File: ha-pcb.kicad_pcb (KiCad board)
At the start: 2 copper layers, 137.2 x 111.8 mm, 52 parts, among them J1 RJ45_NC1W, J10 1VAC_00, J11 1VAC_01, J12 5VCC_02, J13 5VCC_03, J14 30VCC_11, J15 ONOFF_134, J16 I2C_5V, J17 locked, J2 RaPi_Connector, J3 RJ45_NC1W, J4 SainSmart_connector, J5 RJ45_1W1W, J6 RJ45_1W1W, J7 RJ45_1W1W, J8 RJ45_1W1W_T, J9 locked, U1 DMO063_SSR, U10 ADS1115 ADC, U11 ADS1115, U2 PCF_8575, U3 AK-DS2482S-100, U4 Pololu_Level_Shifter, U5 DS18B20, U6 PCA9615_I2C_Diff, U7 AK-DS2482S-100, U8 AK-DS2482S-100, U9 AK-DS2482S-100

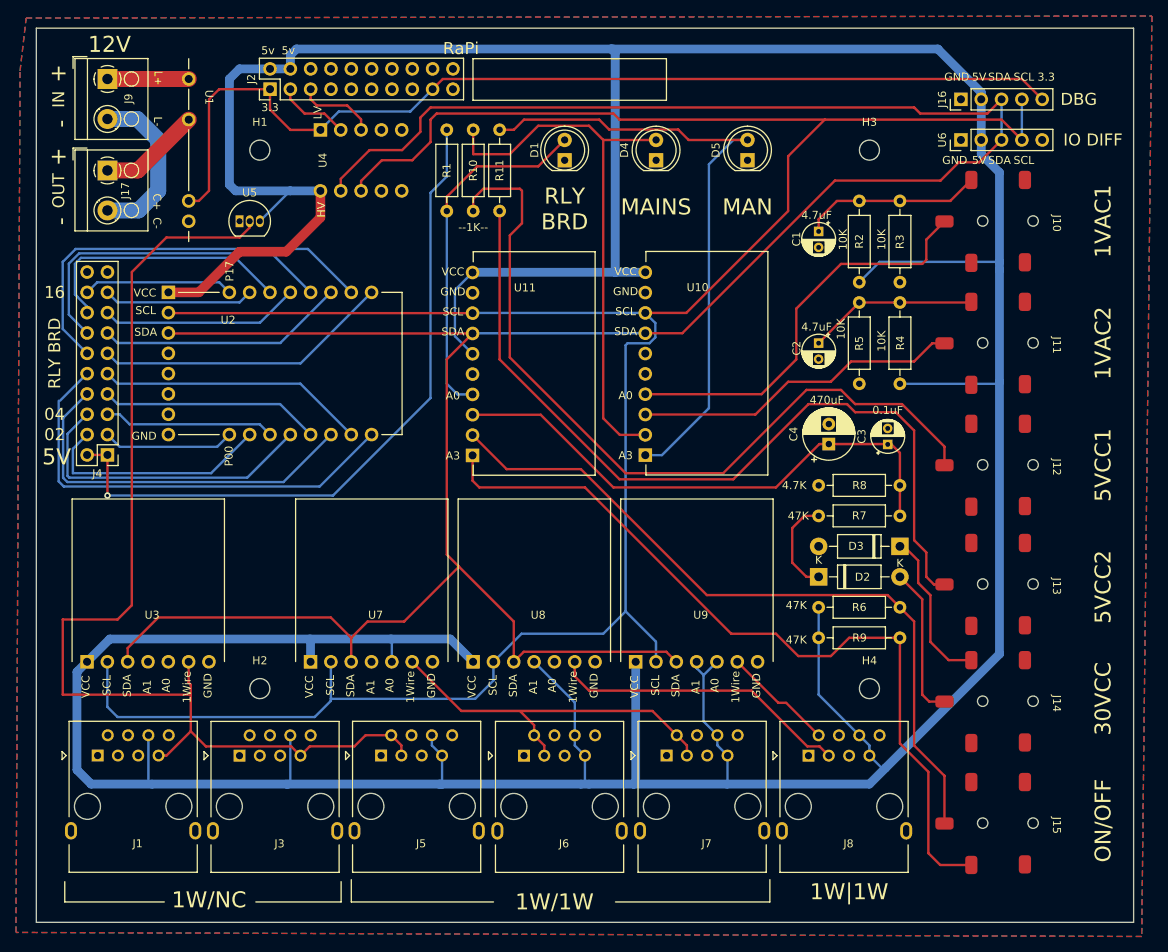
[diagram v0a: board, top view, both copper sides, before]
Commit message: Incorporated feedback from forum.\nAdded two GPIOs for test marking
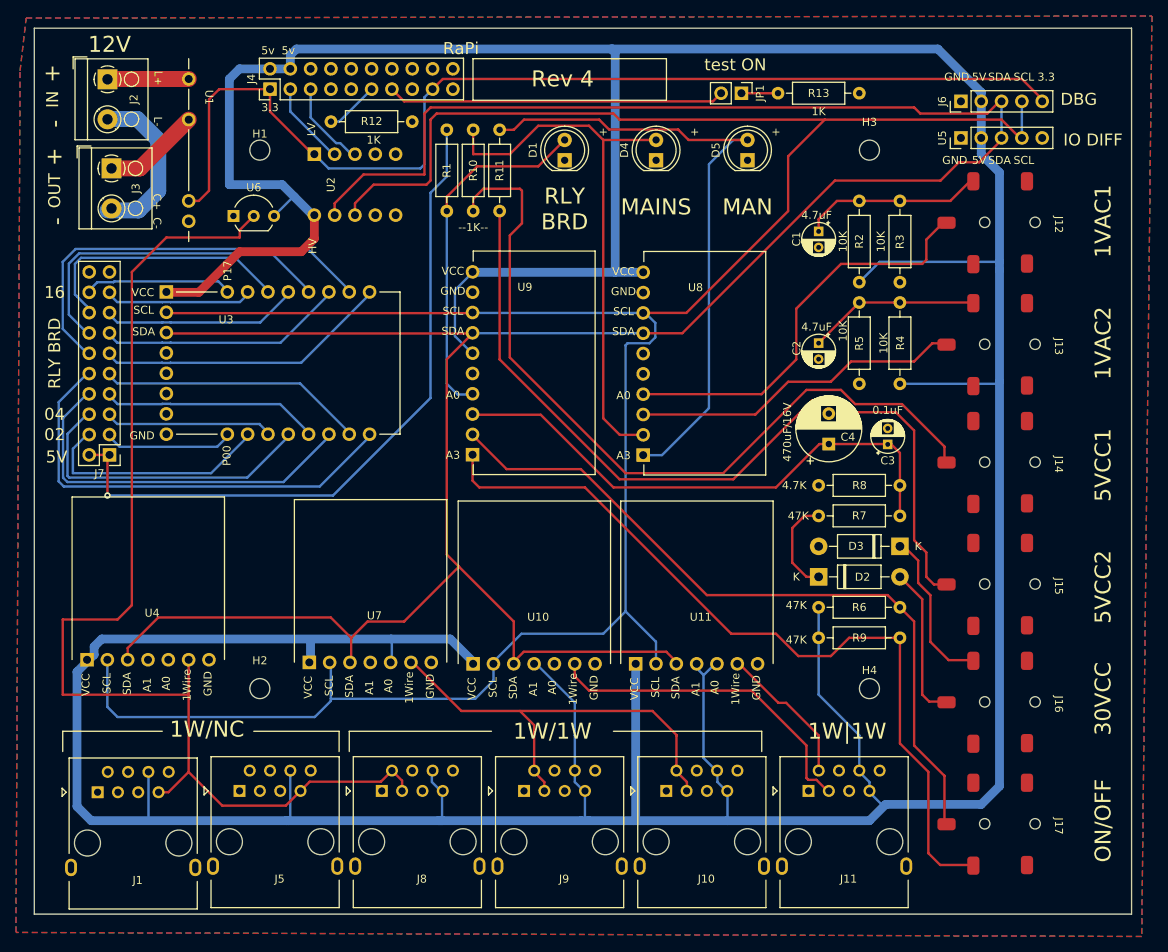
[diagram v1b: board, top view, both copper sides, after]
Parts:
- added JP1: Jumper_2_Open, Connector_PinHeader_2.54mm:PinHeader_1x02_P2.54mm_Vertical, F.Cu at (129.0, 39.6)
- added R12: 1K, Resistor_THT:R_Axial_DIN0207_L6.3mm_D2.5mm_P10.16mm_Horizontal, F.Cu at (77.7, 43.2)
- added R13: 1K, Resistor_THT:R_Axial_DIN0207_L6.3mm_D2.5mm_P10.16mm_Horizontal, F.Cu at (133.6, 39.6)
- C4: value 470uF -> 470uF/16V; footprint Capacitor_THT:CP_Radial_D6.3mm_P2.50mm -> Capacitor_THT:CP_Radial_D8.0mm_P3.80mm
- D1: value yellow -> LED; footprint LED_THT:LED_D5.0mm_IRGrey -> LED_THT:LED_D5.0mm
- D4, D5: value yellow -> LED
- J10: value 1VAC_00 -> RJ45_1W1W; footprint Library:3.5mmJack SMD -> Library:RJ45_Ninigi_GE_silver
- J11: value 1VAC_01 -> RJ45_1W1W; footprint Library:3.5mmJack SMD -> Library:RJ45_Ninigi_GE_silver
- J12: value 5VCC_02 -> 3.5Inch_Audio
- J13: value 5VCC_03 -> 3.5Inch_Audio
- J14: value 30VCC_11 -> 3.5Inch_Audio
- J15: value ONOFF_134 -> 3.5Inch_Audio
- J16: value I2C_5V -> 3.5Inch_Audio; footprint Connector_PinHeader_2.54mm:PinHeader_1x05_P2.54mm_Vertical -> Library:3.5mmJack SMD
- J17: footprint TerminalBlock_RND:TerminalBlock_RND_205-00001_1x02_P5.00mm_Horizontal -> Library:3.5mmJack SMD
- J2: value RaPi_Connector -> 12V IN; footprint Connector_PinHeader_2.54mm:PinHeader_2x10_P2.54mm_Vertical -> TerminalBlock_RND:TerminalBlock_RND_205-00001_1x02_P5.00mm_Horizontal
- J3: value RJ45_NC1W -> 12V OUT; footprint Library:RJ45_Ninigi_GE_silver -> TerminalBlock_RND:TerminalBlock_RND_205-00001_1x02_P5.00mm_Horizontal
- J4: value SainSmart_connector -> RaPi_Connector
- J5: value RJ45_1W1W -> RJ45_NC1W
- J6: value RJ45_1W1W -> Conn_01x05; footprint Library:RJ45_Ninigi_GE_silver -> Connector_PinHeader_2.54mm:PinHeader_1x05_P2.54mm_Vertical
- J7: value RJ45_1W1W -> SainSmart_connector; footprint Library:RJ45_Ninigi_GE_silver -> Connector_PinHeader_2.54mm:PinHeader_2x10_P2.54mm_Vertical
- J8: value RJ45_1W1W_T -> RJ45_1W1W
- J9: footprint TerminalBlock_RND:TerminalBlock_RND_205-00001_1x02_P5.00mm_Horizontal -> Library:RJ45_Ninigi_GE_silver
- U10: value ADS1115 ADC -> AK-DS2482S-100; footprint Library:ADS1115 -> Library:AK-DS2482S-100
- U11: value ADS1115 -> AK-DS2482S-100; footprint Library:ADS1115 -> Library:AK-DS2482S-100
- U2: value PCF_8575 -> Pololu_Level_Shifter; footprint Library:PCF_8575 -> Library:Pololu Level Shifter
- U3: value AK-DS2482S-100 -> PCF_8575; footprint Library:AK-DS2482S-100 -> Library:PCF_8575
- U4: value Pololu_Level_Shifter -> AK-DS2482S-100; footprint Library:Pololu Level Shifter -> Library:AK-DS2482S-100
- U5: value DS18B20 -> PCA9615_I2C_Diff; footprint Package_TO_SOT_THT:TO-92_Inline -> Connector_PinHeader_2.54mm:PinHeader_1x05_P2.54mm_Vertical
- U6: value PCA9615_I2C_Diff -> DS18B20; footprint Connector_PinHeader_2.54mm:PinHeader_1x05_P2.54mm_Vertical -> Package_TO_SOT_THT:TO-92_Inline_Wide
- U8, U9: value AK-DS2482S-100 -> ADS1115; footprint Library:AK-DS2482S-100 -> Library:ADS1115
- moved J17 137.8 mm to (167.8, 120.5)
- moved J9 103.1 mm to (101.9, 126.8), turned to 0 degrees
- moved J6 98.3 mm to (156.5, 40.6), turned to 90 degrees
- moved J10 94.7 mm to (119.6, 126.8), turned to 0 degrees
- moved U6 91.4 mm to (65.5, 55.0), turned to 0 degrees
- moved U5 90.8 mm to (156.5, 45.2), turned to 90 degrees
- moved J7 79.1 mm to (50.0, 84.8), turned to 180 degrees
- moved J3 75.1 mm to (50.3, 49.0), turned to -90 degrees
- moved J11 73.0 mm to (137.4, 126.8), turned to 0 degrees
- moved J16 65.8 mm to (167.8, 105.2), turned to -90 degrees
- moved J8 53.5 mm to (84.1, 126.8)
- moved J4 50.0 mm to (70.1, 39.1), turned to 90 degrees
- moved U4 47.5 mm to (45.4, 90.1), turned to 0 degrees
- moved U11 37.6 mm to (113.9, 90.6)
- moved U10 37.6 mm to (93.6, 90.6)
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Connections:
- C3 pad 1: Net-(C3-Pad1) -> /A2/1
- C4 pad 1: Net-(C3-Pad1) -> /A2/1
- D1 pad 2: /5VRB -> /A2/0
- D4 pad 2: Net-(D4-Pad2) -> /A1/2
- D5 pad 2: Net-(D5-Pad2) -> /A1/3
- J1 pad SH: (no net) -> GND
- J10 pad 1: Net-(C1-Pad1) -> GND
- J10 pad 3: unconnected-(J10-Pad3) -> Net-(J10-Pad2)
- J10 pad 4: (no net) -> GND
- J10 pad 5: (no net) -> GND
- J11 pad 1: Net-(C2-Pad1) -> GND
- J11 pad 3: unconnected-(J11-Pad3) -> Net-(J11-Pad3)
- J11 pad 4: (no net) -> GND
- J11 pad 5: (no net) -> GND
- J12 pad 1: GND -> Net-(C1-Pad1)
- J12 pad 2: Net-(J12-Pad2) -> /A1/0
- J12 pad 4: (no net) -> GND
- J12 pad 5: (no net) -> GND
- J13 pad 1: GND -> Net-(C2-Pad1)
- J13 pad 2: Net-(J13-Pad2) -> /A1/1
- J13 pad 4: (no net) -> GND
- J13 pad 5: (no net) -> GND
- J14 pad 1: Net-(D3-Pad1) -> GND
- J14 pad 2: Net-(D2-Pad2) -> Net-(J14-Pad2)
- J14 pad 4: (no net) -> GND
- J14 pad 5: (no net) -> GND
- J15 pad 3: Net-(J15-Pad3) -> unconnected-(J15-Pad3)
- J15 pad 4: (no net) -> GND
- J15 pad 5: (no net) -> GND
- J16 pad 1: GND -> Net-(D3-Pad1)
- J16 pad 2: +5V -> Net-(D2-Pad2)
- J16 pad 3: /SDA -> unconnected-(J16-Pad3)
- J16 pad 4: /SCL -> GND
- J16 pad 5: /+3.3V -> GND
- J17 pad 1: Net-(J17-Pad1) -> GND
- J17 pad 2: Net-(J17-Pad2) -> /A2/2
- J2 pad 1: /+3.3V -> Net-(J2-Pad1)
- J2 pad 2: +5V -> Net-(J2-Pad2)
- J3 pad 1: unconnected-(J3-Pad1) -> Net-(J3-Pad1)
- J3 pad 2: unconnected-(J3-Pad2) -> Net-(J2-Pad2)
- J4 pad 1: /5VSS -> /+3.3V
- J4 pad 10: Net-(J4-Pad10) -> unconnected-(J4-Pad10)
- J4 pad 12: Net-(J4-Pad12) -> unconnected-(J4-Pad12)
- J4 pad 14: Net-(J4-Pad14) -> GND
- J4 pad 15: Net-(J4-Pad15) -> unconnected-(J4-Pad15)
- J4 pad 16: Net-(J4-Pad16) -> unconnected-(J4-Pad16)
- J4 pad 17: /R15 -> /+3.3V
- J4 pad 18: /R16 -> unconnected-(J4-Pad18)
- J4 pad 19: GND -> unconnected-(J4-Pad19)
- J4 pad 2: /5VSS -> +5V
- J4 pad 3: /R01 -> /SDA_L
- J4 pad 4: /R02 -> +5V
- J4 pad 5: Net-(J4-Pad5) -> /SCL_L
- J4 pad 6: Net-(J4-Pad6) -> GND
- J4 pad 7: Net-(J4-Pad7) -> unconnected-(J4-Pad7)
- J4 pad 8: Net-(J4-Pad8) -> unconnected-(J4-Pad8)
- J4 pad 9: Net-(J4-Pad9) -> GND
- J5 pad 1: GND -> unconnected-(J5-Pad1)
- J5 pad 2: Net-(J1-Pad7) -> unconnected-(J5-Pad2)
- J5 pad 3: Net-(J1-Pad7) -> unconnected-(J5-Pad3)
- J5 pad 4: GND -> unconnected-(J5-Pad4)
- J5 pad 7: +5V -> Net-(J1-Pad7)
- J5 pad SH: (no net) -> GND
- J6 pad 2: Net-(J6-Pad2) -> +5V
- J6 pad 3: Net-(J6-Pad2) -> /SDA
- J6 pad 4: GND -> /SCL
- J6 pad 5: GND -> /+3.3V
- J7 pad 1: GND -> /5VSS
- J7 pad 2: Net-(J6-Pad2) -> /5VSS
- J7 pad 3: Net-(J6-Pad2) -> /R01
- J7 pad 4: GND -> /R02
- J7 pad 5: GND -> Net-(J7-Pad5)
- J7 pad 6: +5V -> Net-(J7-Pad6)
- J7 pad 7: +5V -> Net-(J7-Pad7)
- J7 pad 8: GND -> Net-(J7-Pad8)
- J8 pad 2: Net-(J8-Pad2) -> Net-(J1-Pad7)
- J8 pad 3: Net-(J8-Pad3) -> Net-(J1-Pad7)
- J8 pad SH: (no net) -> GND
- J9 pad 1: Net-(J9-Pad1) -> GND
- J9 pad 2: Net-(J17-Pad2) -> Net-(J10-Pad2)
- R1 pad 2: /5VRB -> /A2/0
- R10 pad 1: Net-(D4-Pad2) -> /A1/2
- R10 pad 2: Net-(J12-Pad2) -> Net-(J14-Pad2)
- R11 pad 1: Net-(D5-Pad2) -> /A1/3
- R11 pad 2: Net-(J13-Pad2) -> Net-(J15-Pad2)
- R6 pad 1: Net-(J15-Pad2) -> /A2/2
- R7 pad 1: Net-(C3-Pad1) -> /A2/1
- R8 pad 2: Net-(C3-Pad1) -> /A2/1
- R9 pad 1: Net-(J15-Pad3) -> /A2/3
- U1 pad 1: Net-(J9-Pad1) -> Net-(J2-Pad1)
- U1 pad 2: Net-(J17-Pad1) -> Net-(J3-Pad1)
- U10 pad 1: Net-(D5-Pad2) -> +5V
- U10 pad 2: Net-(D4-Pad2) -> /SCL
- U10 pad 3: Net-(J11-Pad2) -> /SDA
- U10 pad 4: Net-(J10-Pad2) -> +5V
- U10 pad 6: GND -> Net-(J11-Pad3)
- U10 pad 7: /SDA -> GND
- U11 pad 1: Net-(J15-Pad3) -> +5V
- U11 pad 2: Net-(J15-Pad2) -> /SCL
- U11 pad 3: Net-(C3-Pad1) -> /SDA
- U11 pad 4: /5VRB -> +5V
- U11 pad 5: unconnected-(U11-Pad5) -> +5V
- U11 pad 6: +5V -> Net-(J11-Pad2)
- U11 pad 7: /SDA -> GND
- U2 pad 1: +5V -> /+3.3V
- U2 pad 10: /R02 -> unconnected-(U2-Pad10)
- U2 pad 2: /SCL -> /SDA_L
- U2 pad 3: /SDA -> /SCL_L
- U2 pad 4: GND -> unconnected-(U2-Pad4)
- U2 pad 5: GND -> unconnected-(U2-Pad5)
- U2 pad 6: GND -> +5V
- U2 pad 7: unconnected-(U2-Pad7) -> /SDA
- U2 pad 8: GND -> /SCL
- U2 pad 9: /R01 -> unconnected-(U2-Pad9)
- U3 pad 4: unconnected-(U3-Pad4) -> GND
- U3 pad 5: unconnected-(U3-Pad5) -> GND
- U3 pad 6: Net-(J1-Pad7) -> GND
- U3 pad 7: GND -> unconnected-(U3-Pad7)
- U4 pad 1: /+3.3V -> +5V
- U4 pad 2: /SDA_L -> /SCL
- U4 pad 3: /SCL_L -> /SDA
- U4 pad 6: +5V -> Net-(J1-Pad7)
- U4 pad 7: /SDA -> GND
- U5 pad 2: Net-(J1-Pad7) -> +5V
- U5 pad 3: +5V -> /SDA
- U6 pad 2: +5V -> Net-(J1-Pad7)
- U6 pad 3: /SDA -> +5V
- U7 pad 6: Net-(J6-Pad2) -> Net-(J10-Pad2)
- U8 pad 1: +5V -> /A1/3
- U8 pad 2: /SCL -> /A1/2
- U8 pad 3: /SDA -> /A1/1
- U8 pad 4: +5V -> /A1/0
- U8 pad 6: Net-(J8-Pad3) -> GND
- U8 pad 7: GND -> /SDA
- U9 pad 1: +5V -> /A2/3
- U9 pad 2: /SCL -> /A2/2
- U9 pad 3: /SDA -> /A2/1
- U9 pad 4: +5V -> /A2/0
- U9 pad 5: +5V -> unconnected-(U9-Pad5)
- U9 pad 6: Net-(J8-Pad2) -> +5V
- U9 pad 7: GND -> /SDA
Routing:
- net Net-(J13-Pad2): track 103.4 -> 0.00 mm
- net Net-(J15-Pad3): track 101.0 -> 0.00 mm
- net /A2/3: track 0.00 -> 101.0 mm
- net Net-(J14-Pad2): track 0.00 -> 99.6 mm
- net Net-(J12-Pad2): track 99.6 -> 0.00 mm
- net /A2/2: track 0.00 -> 91.7 mm
- net Net-(D5-Pad2): track 79.5 -> 0.00 mm
- net /A1/3: track 0.00 -> 79.5 mm
- net Net-(D4-Pad2): track 69.0 -> 0.00 mm
- net /A1/2: track 0.00 -> 69.0 mm
- net Net-(C3-Pad1): track 67.8 -> 0.00 mm
- net /A2/1: track 0.00 -> 67.8 mm
- net Net-(J7-Pad10): track 0.00 -> 57.4 mm
- net Net-(J4-Pad10): track 57.0 -> 0.00 mm
- net Net-(J7-Pad12): track 0.00 -> 51.7 mm
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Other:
- board size 137.2 x 111.8 mm -> 137.2 x 110.7 mm
- board text added: "Rev 4"
- board text added: "test ON"
- board text removed: "10K"
